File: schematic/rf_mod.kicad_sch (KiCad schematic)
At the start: 31 parts, among them J4A Conn_01x08, Q3 2N3906, Q6 2N3906, U23 4066

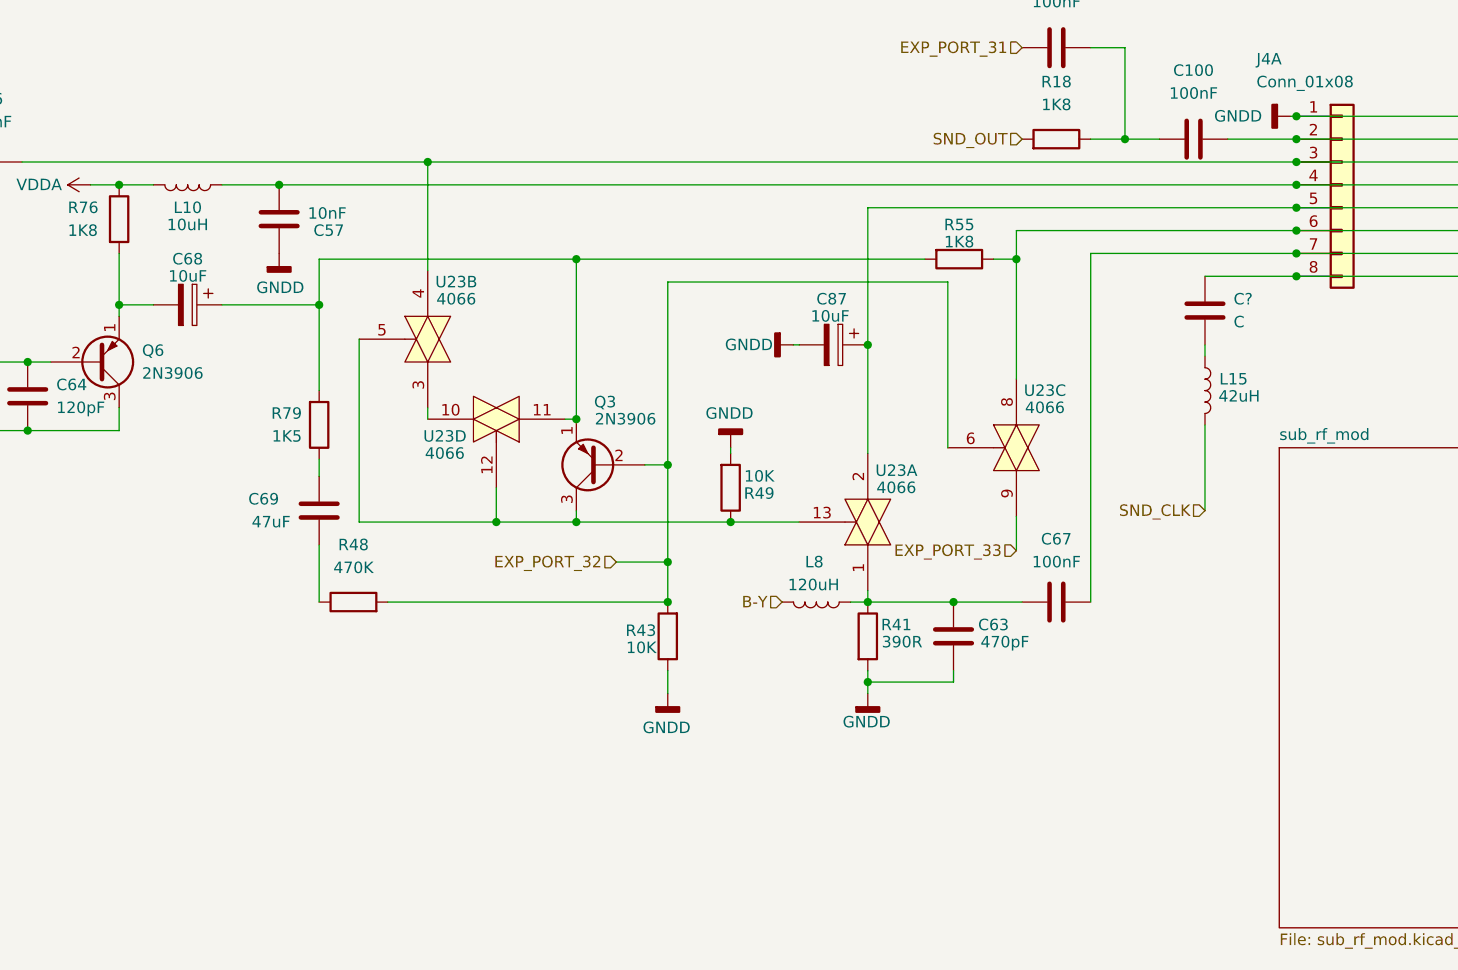
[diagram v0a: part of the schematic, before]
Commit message: cleanup of power supply, and another pass at the RF circuit. Both look much better. The RF circuit just looks wrong though. Will need to check it over.
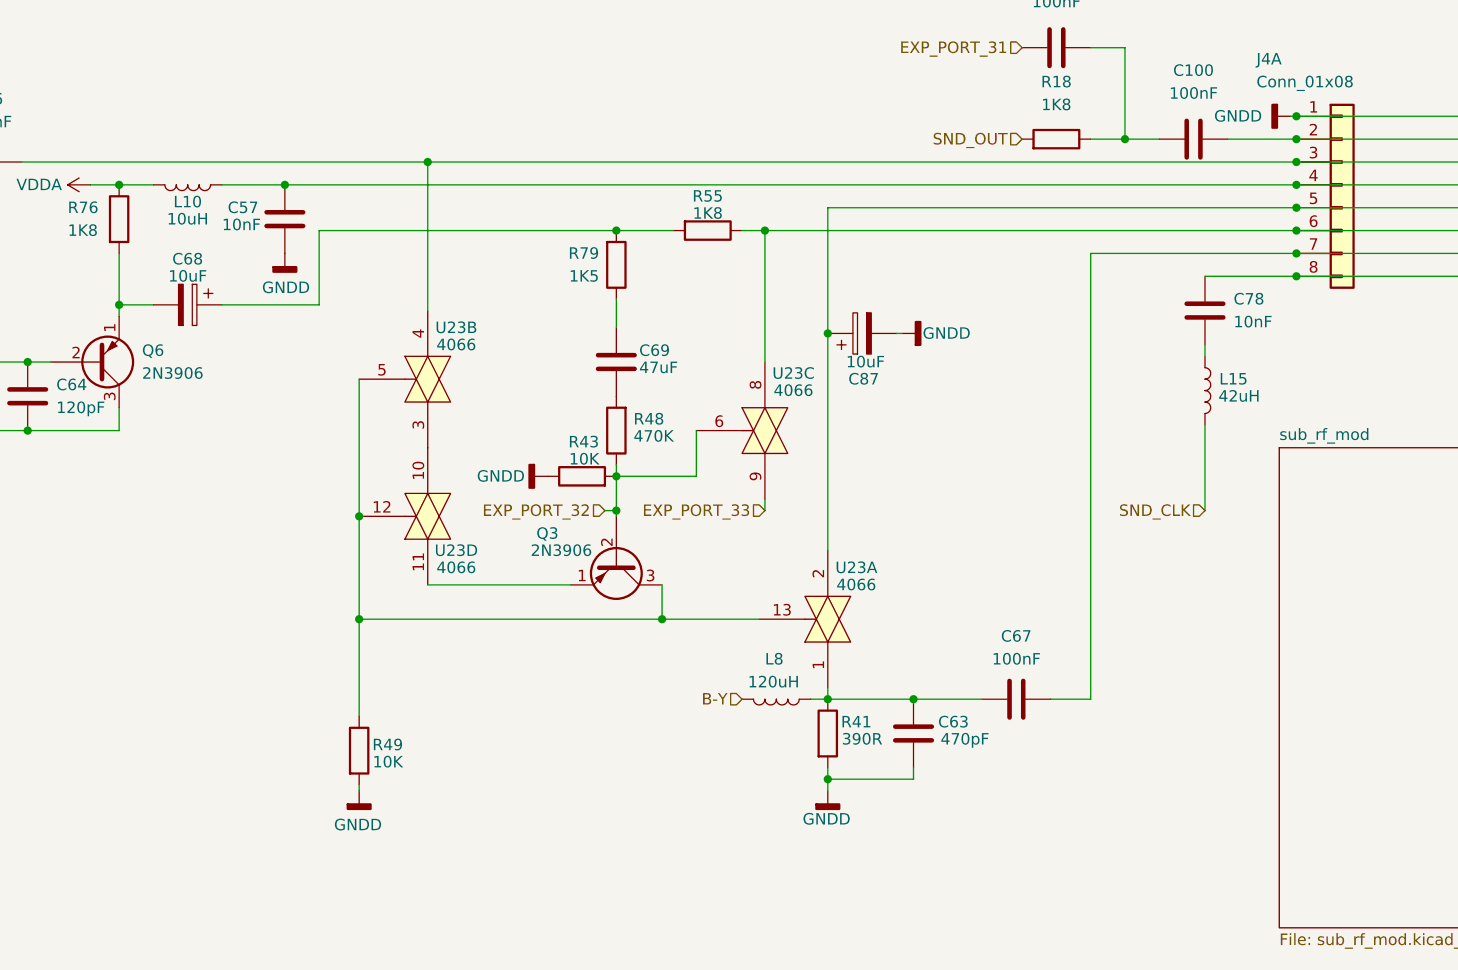
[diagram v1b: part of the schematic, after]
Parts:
- C78: renamed from C?; value C -> 10nF
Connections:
- net EXP_PORT_32: now also R48.1; no longer R48.2
- net at C69.1: now also R48.2; no longer R48.1
- net at C68.1, R55.2, R79.2: no longer Q3.1 (E), U23.11
- new net: Q3.1 (E), U23.11
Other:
- moved on the sheet: C57, C63, C67, C69, C87, L8, Q3, R41, R43, R48, R49, R55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

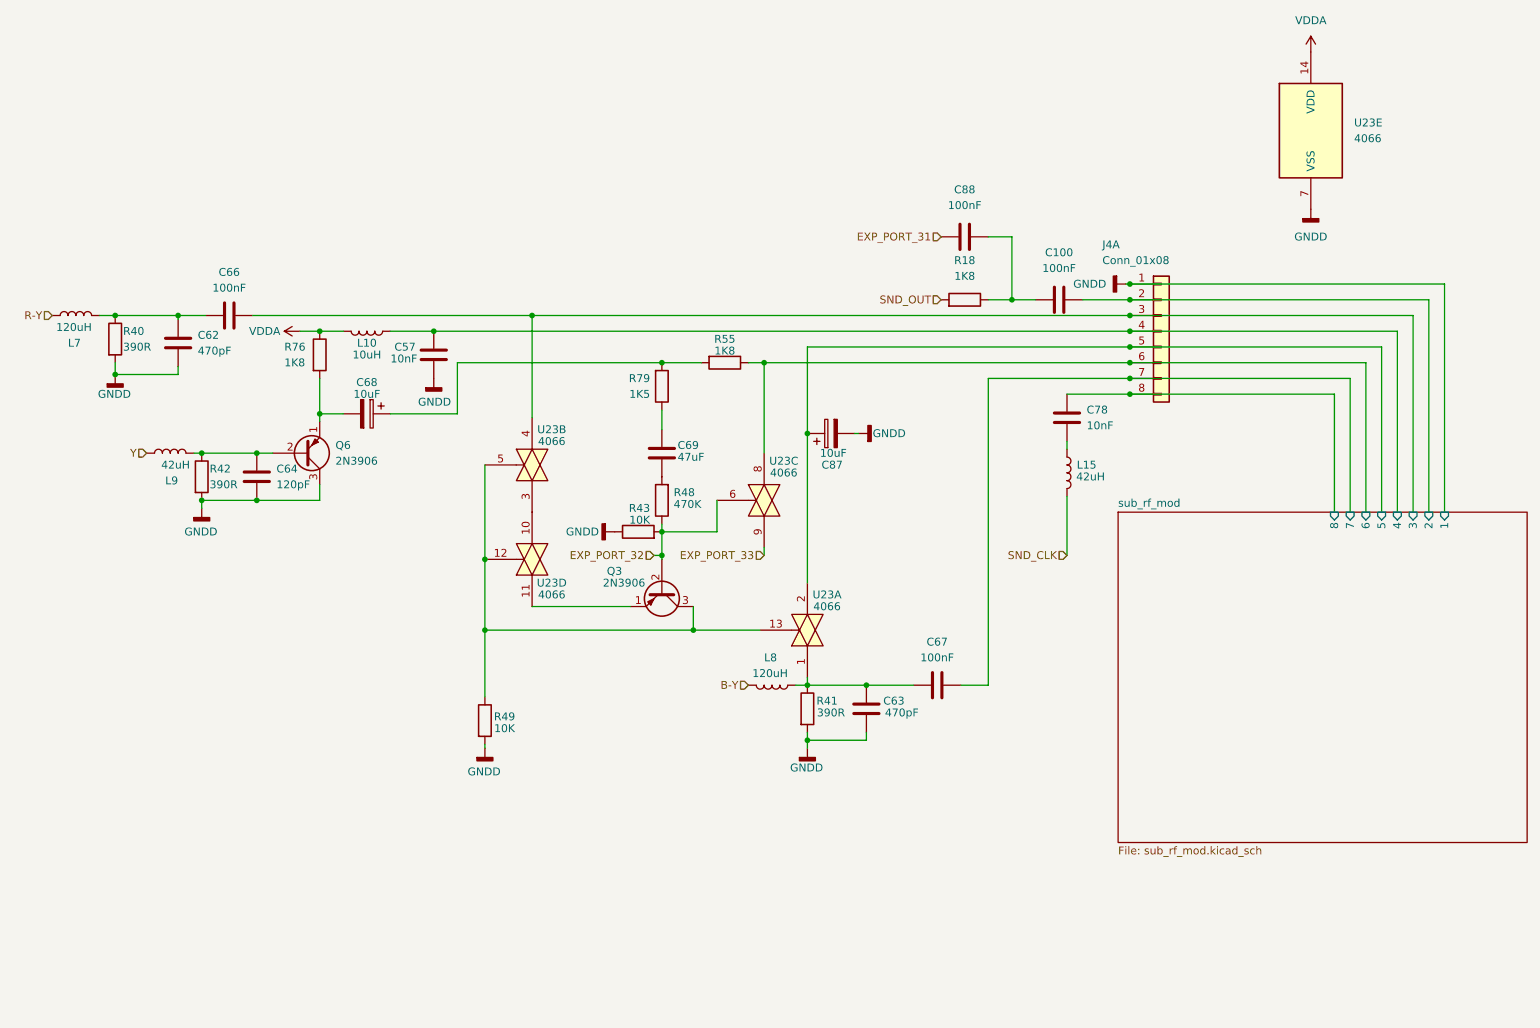
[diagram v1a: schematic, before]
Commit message: cleaned up RF circuit again, and used ChildOfCv schematic as a ref. Fixed a few mistakes. I didn't know his even existed. Its a very nice project. I didn't know it existed till I was googling some sources for the RF part, since the ADAM was different. Though his RF circuit for the daughter board is different in ways that don't make sense for mine. I'll have to double check that by hand.
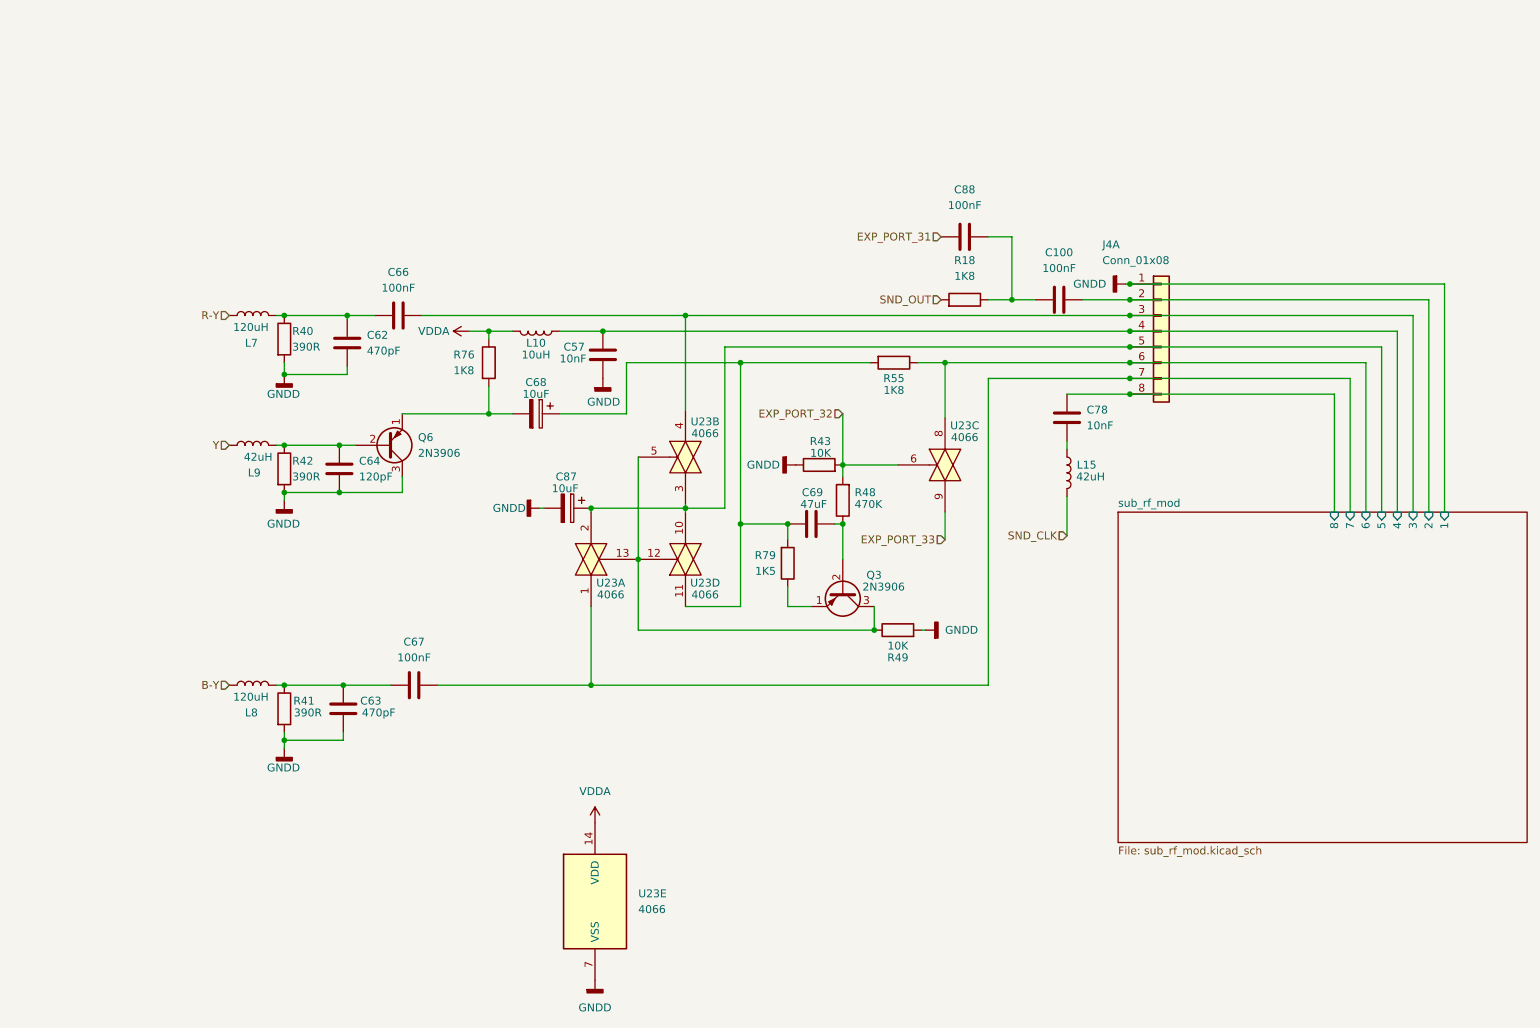
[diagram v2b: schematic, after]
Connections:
- net EXP_PORT_32: now also R48.2; no longer Q3.2 (B), R48.1
- net sub_rf_mod/5: now also U23.10, U23.3
- net sub_rf_mod/7: now also U23.1
- net at C69.1: now also Q3.2 (B), R48.1; no longer R48.2
- net at C63.1, C67.1, L8.1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: no longer U23.1
- net at C68.1, R55.2, R79.2: now also C69.2, U23.11
- net at R79.1: now also Q3.1 (E); no longer C69.2
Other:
- moved on the sheet: C57, C62, C63, C64, C66, C67, C68, C69, C87, L10, L7, L8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

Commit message: all lines renamed, based most of the names from the coleco adam schematic. CS cart lines are my own, and the rest are from the wiki schematic for the controller... those will need to be checked.
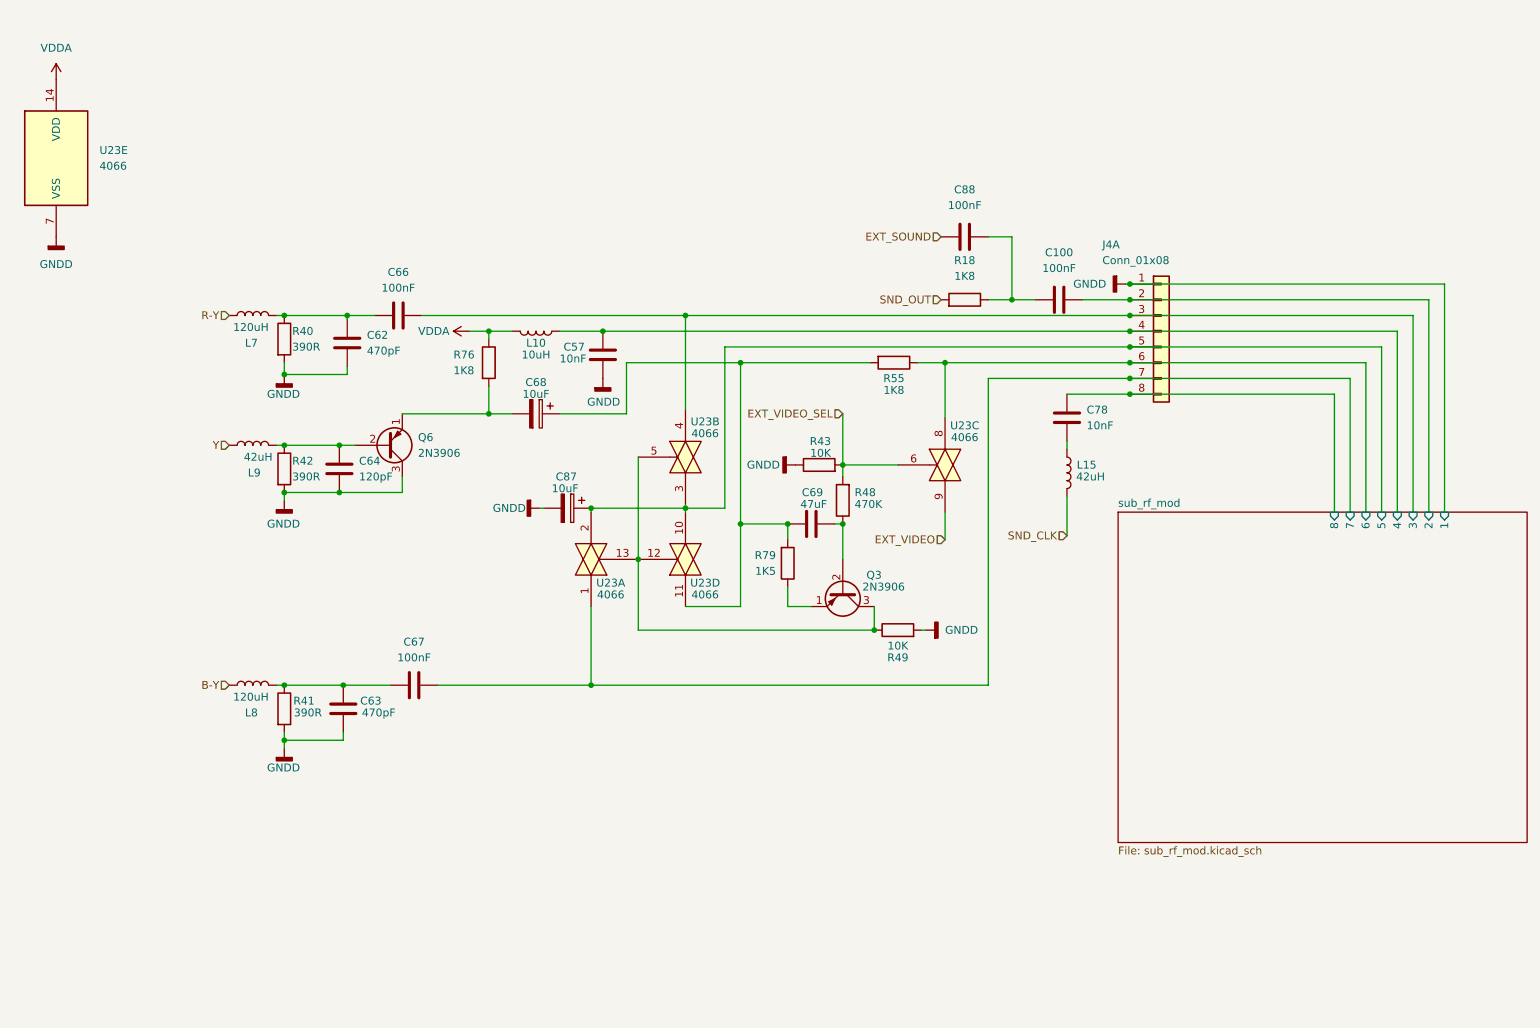
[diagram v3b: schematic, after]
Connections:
- net EXP_PORT_31 renamed EXT_SOUND
- net EXP_PORT_32 renamed EXT_VIDEO_SEL
- net EXP_PORT_33 renamed EXT_VIDEO
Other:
- moved on the sheet: U23E
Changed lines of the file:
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@@
     (effects (font (size 1.27 1.27)) (justify right))
   )
-  (hierarchical_label "EXP_PORT_31" (shape input) (at 175.26 52.705 180)
+  (hierarchical_label "EXT_SOUND" (shape input) (at 175.26 52.705 180)
     (effects (font (size 1.27 1.27)) (justify right))
   )
@@
     (effects (font (size 1.27 1.27)) (justify right))
   )
-  (hierarchical_label "EXP_PORT_33" (shape input) (at 175.895 101.6 180)
+  (hierarchical_label "EXT_VIDEO" (shape input) (at 175.895 101.6 180)
     (effects (font (size 1.27 1.27)) (justify right))
   )
@@
     (effects (font (size 1.27 1.27)) (justify right))
   )
-  (hierarchical_label "EXP_PORT_32" (shape input) (at 159.385 81.28 180)
+  (hierarchical_label "EXT_VIDEO_SEL" (shape input) (at 159.385 81.28 180)
     (effects (font (size 1.27 1.27)) (justify right))
   )
@@
     (pin "2")
   )
-  (symbol (lib_id "4xxx:4066") (at 119.38 160.02 0) (unit 5)
-    (in_bom yes) (on_board yes) (fields_autoplaced)
-    (property "Reference" "U23" (id 0) (at 126.365 158.7499 0)
-      (effects (font (size 1.27 1.27)) (justify left))
-    )
-    (property "Value" "4066" (id 1) (at 126.365 161.2899 0)
-      (effects (font (size 1.27 1.27)) (justify left))
-    )
-    (property "Footprint" "" (id 2) (at 119.38 160.02 0)
-      (effects (font (size 1.27 1.27)) hide)
-    )
-    (property "Datasheet" "http://www.ti.com/lit/ds/symlink/cd4066b.pdf" (id 3) (at 119.38 160.02 0)
+  (symbol (lib_id "4xxx:4066") (at 32.385 40.005 0) (unit 5)
+    (in_bom yes) (on_board yes) (fields_autoplaced)
+    (property "Reference" "U23" (id 0) (at 39.37 38.7349 0)
+      (effects (font (size 1.27 1.27)) (justify left))
+    )
+    (property "Value" "4066" (id 1) (at 39.37 41.2749 0)
+      (effects (font (size 1.27 1.27)) (justify left))
+    )
+    (property "Footprint" "" (id 2) (at 32.385 40.005 0)
+      (effects (font (size 1.27 1.27)) hide)
+    )
+    (property "Datasheet" "http://www.ti.com/lit/ds/symlink/cd4066b.pdf" (id 3) (at 32.385 40.005 0)
       (effects (font (size 1.27 1.27)) hide)
     )
@@
     (pin "2")
   )
-  (symbol (lib_id "power:VDDA") (at 119.38 147.32 0) (unit 1)
-    (in_bom yes) (on_board yes) (fields_autoplaced)
-    (property "Reference" "#PWR?" (id 0) (at 119.38 151.13 0)
-      (effects (font (size 1.27 1.27)) hide)
-    )
-    (property "Value" "VDDA" (id 1) (at 119.38 142.24 0))
-    (property "Footprint" "" (id 2) (at 119.38 147.32 0)
-      (effects (font (size 1.27 1.27)) hide)
-    )
-    (property "Datasheet" "" (id 3) (at 119.38 147.32 0)
+  (symbol (lib_id "power:VDDA") (at 32.385 27.305 0) (unit 1)
+    (in_bom yes) (on_board yes) (fields_autoplaced)
+    (property "Reference" "#PWR?" (id 0) (at 32.385 31.115 0)
+      (effects (font (size 1.27 1.27)) hide)
+    )
+    (property "Value" "VDDA" (id 1) (at 32.385 22.225 0))
+    (property "Footprint" "" (id 2) (at 32.385 27.305 0)
+      (effects (font (size 1.27 1.27)) hide)
+    )
+    (property "Datasheet" "" (id 3) (at 32.385 27.305 0)
       (effects (font (size 1.27 1.27)) hide)
     )
@@
     (pin "3")
   )
-  (symbol (lib_id "power:GNDD") (at 119.38 172.72 0) (unit 1)
-    (in_bom yes) (on_board yes) (fields_autoplaced)
-    (property "Reference" "#PWR?" (id 0) (at 119.38 179.07 0)
-      (effects (font (size 1.27 1.27)) hide)
-    )
-    (property "Value" "GNDD" (id 1) (at 119.38 177.165 0))
-    (property "Footprint" "" (id 2) (at 119.38 172.72 0)
-      (effects (font (size 1.27 1.27)) hide)
-    )
-    (property "Datasheet" "" (id 3) (at 119.38 172.72 0)
-      (effects (font (size 1.27 1.27)) hide)
-    )
+  (symbol (lib_id "power:GNDD") (at 32.385 52.705 0) (unit 1)
+    (in_bom yes) (on_board yes) (fields_autoplaced)
+    (property "Reference" "#PWR?" (id 0) (at 32.385 59.055 0)
+      (effects (font (size 1.27 1.27)) hide)
+    )
+    (property "Value" "GNDD" (id 1) (at 32.385 57.15 0))
+    (property "Footprint" "" (id 2) (at 32.385 52.705 0)
+      (effects (font (size 1.27 1.27)) hide)
+    )
+    (property "Datasheet" "" (id 3) (at 32.385 52.705 0)
+      (effects (font (size 1.27 1.27)) hide)
+    )
